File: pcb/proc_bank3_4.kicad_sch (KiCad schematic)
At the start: 2 parts, among them U1 XC6SLX9-TQG144

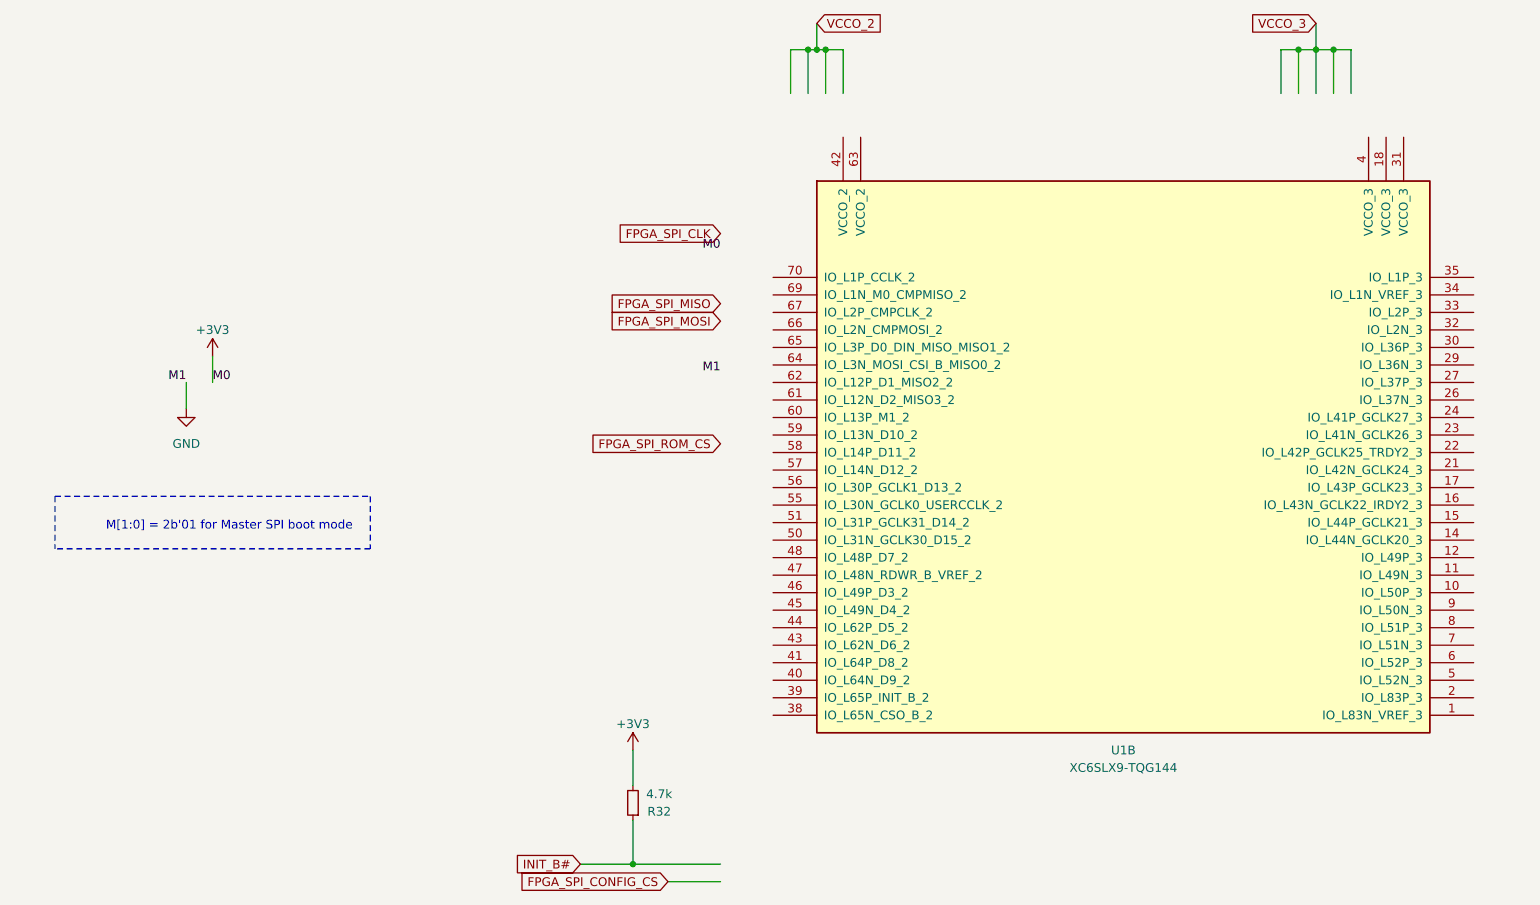
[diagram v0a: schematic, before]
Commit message: route pol
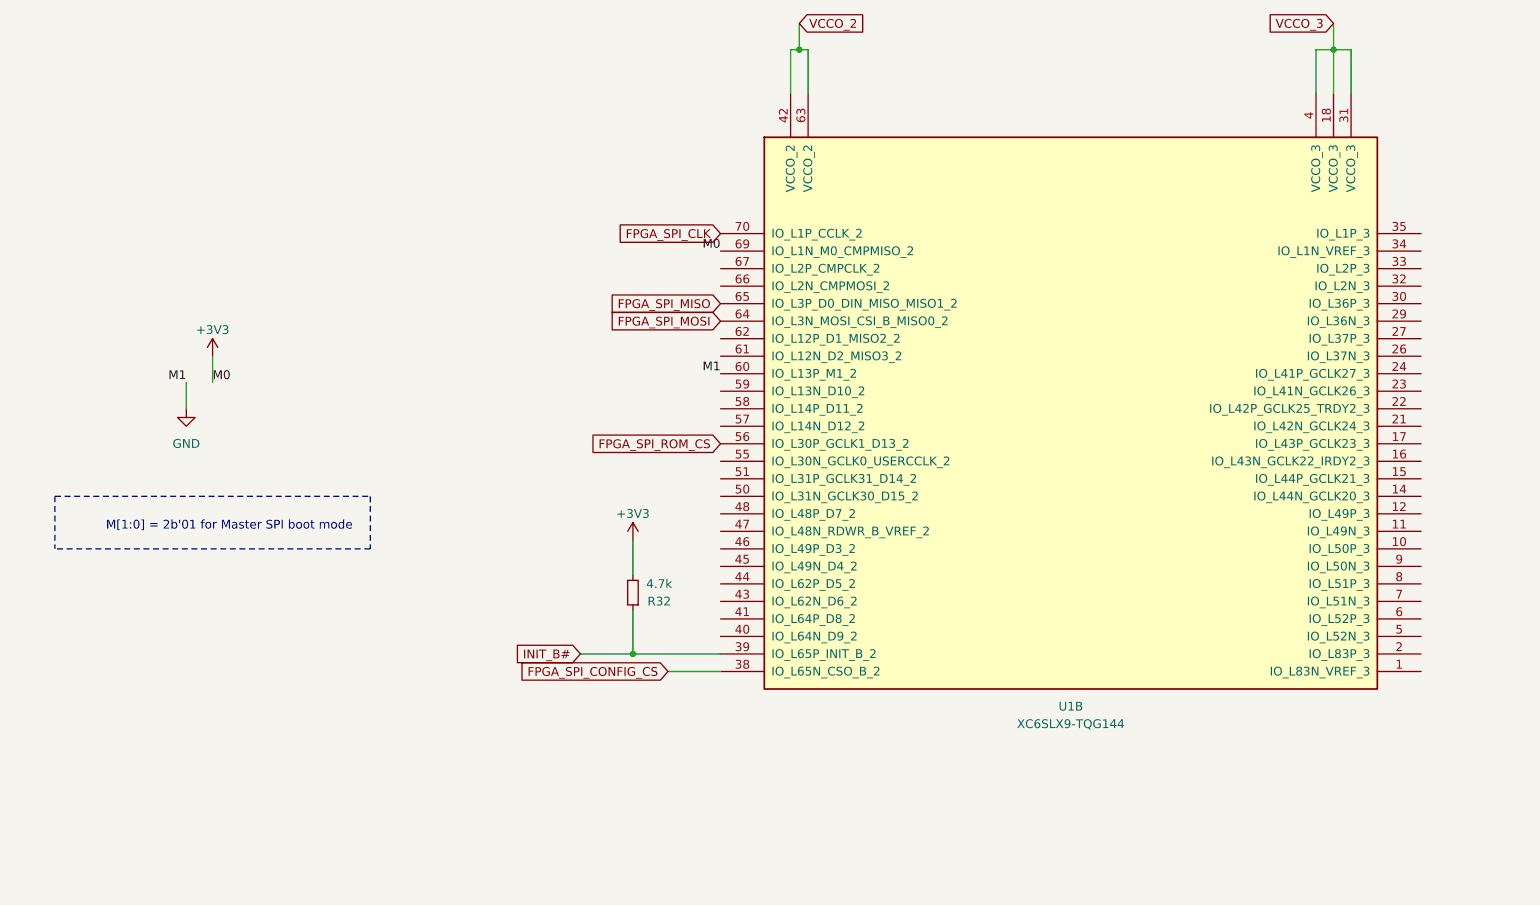
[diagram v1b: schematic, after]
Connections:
- net +3V3: now also U1.69 (IO_L1N_M0_CMPMISO_2)
- net FPGA_SPI_CLK: now also U1.70 (IO_L1P_CCLK_2)
- net FPGA_SPI_CONFIG_CS: now also U1.38 (IO_L65N_CSO_B_2)
- net FPGA_SPI_MISO: now also U1.65 (IO_L3P_D0_DIN_MISO_MISO1_2)
- net FPGA_SPI_MOSI: now also U1.64 (IO_L3N_MOSI_CSI_B_MISO0_2)
- net FPGA_SPI_ROM_CS: now also U1.56 (IO_L30P_GCLK1_D13_2)
- net GND: now also U1.60 (IO_L13P_M1_2)
- net INIT_B#: now also U1.39 (IO_L65P_INIT_B_2)
- net VCCO_2: now also U1.42 (VCCO_2), U1.63 (VCCO_2)
- net VCCO_3: now also U1.18 (VCCO_3), U1.31 (VCCO_3), U1.4 (VCCO_3)
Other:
- moved on the sheet: R32, U1B
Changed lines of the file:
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@@
 (kicad_sch (version 20210406) (generator eeschema)
-  (paper "User" 280.01 240.005)
-  (junction (at 121.92 147.32) (diameter 0.9144) (color 0 0 0 0))
-  (junction (at 147.32 29.21) (diameter 0.9144) (color 0 0 0 0))
-  (junction (at 148.59 29.21) (diameter 0.9144) (color 0 0 0 0))
-  (junction (at 149.86 29.21) (diameter 0.9144) (color 0 0 0 0))
-  (junction (at 218.44 29.21) (diameter 0.9144) (color 0 0 0 0))
-  (junction (at 220.98 29.21) (diameter 0.9144) (color 0 0 0 0))
+  (paper "User" 280.01 180.01)
+  (junction (at 121.92 116.84) (diameter 0.9144) (color 0 0 0 0))
+  (junction (at 146.05 29.21) (diameter 0.9144) (color 0 0 0 0))
   (junction (at 223.52 29.21) (diameter 0.9144) (color 0 0 0 0))
   (wire (pts (xy 57.15 77.47) (xy 57.15 81.28))
@@
     (stroke (width 0) (type solid) (color 0 0 0 0))
   )
-  (wire (pts (xy 114.3 147.32) (xy 121.92 147.32))
+  (wire (pts (xy 114.3 116.84) (xy 121.92 116.84))
     (stroke (width 0) (type solid) (color 0 0 0 0))
   )
-  (wire (pts (xy 121.92 130.81) (xy 121.92 135.89))
+  (wire (pts (xy 121.92 100.33) (xy 121.92 105.41))
     (stroke (width 0) (type solid) (color 0 0 0 0))
   )
-  (wire (pts (xy 121.92 147.32) (xy 121.92 140.97))
+  (wire (pts (xy 121.92 116.84) (xy 121.92 110.49))
     (stroke (width 0) (type solid) (color 0 0 0 0))
   )
-  (wire (pts (xy 127 149.86) (xy 134.62 149.86))
+  (wire (pts (xy 127 119.38) (xy 134.62 119.38))
     (stroke (width 0) (type solid) (color 0 0 0 0))
   )
-  (wire (pts (xy 134.62 147.32) (xy 121.92 147.32))
+  (wire (pts (xy 134.62 116.84) (xy 121.92 116.84))
     (stroke (width 0) (type solid) (color 0 0 0 0))
   )
-  (wire (pts (xy 144.78 29.21) (xy 147.32 29.21))
+  (wire (pts (xy 144.78 29.21) (xy 146.05 29.21))
     (stroke (width 0) (type solid) (color 0 0 0 0))
   )
@@
     (stroke (width 0) (type solid) (color 0 0 0 0))
   )
-  (wire (pts (xy 147.32 29.21) (xy 147.32 35.56))
+  (wire (pts (xy 146.05 25.4) (xy 146.05 29.21))
     (stroke (width 0) (type solid) (color 0 0 0 0))
   )
-  (wire (pts (xy 147.32 29.21) (xy 148.59 29.21))
+  (wire (pts (xy 146.05 29.21) (xy 147.32 29.21))
     (stroke (width 0) (type solid) (color 0 0 0 0))
   )
-  (wire (pts (xy 148.59 25.4) (xy 148.59 29.21))
-    (stroke (width 0) (type solid) (color 0 0 0 0))
-  )
-  (wire (pts (xy 149.86 29.21) (xy 148.59 29.21))
-    (stroke (width 0) (type solid) (color 0 0 0 0))
-  )
-  (wire (pts (xy 149.86 29.21) (xy 149.86 35.56))
-    (stroke (width 0) (type solid) (color 0 0 0 0))
-  )
-  (wire (pts (xy 149.86 29.21) (xy 152.4 29.21))
-    (stroke (width 0) (type solid) (color 0 0 0 0))
-  )
-  (wire (pts (xy 152.4 35.56) (xy 152.4 29.21))
-    (stroke (width 0) (type solid) (color 0 0 0 0))
-  )
-  (wire (pts (xy 215.9 29.21) (xy 215.9 35.56))
-    (stroke (width 0) (type solid) (color 0 0 0 0))
-  )
-  (wire (pts (xy 215.9 29.21) (xy 218.44 29.21))
-    (stroke (width 0) (type solid) (color 0 0 0 0))
-  )
-  (wire (pts (xy 218.44 29.21) (xy 218.44 35.56))
-    (stroke (width 0) (type solid) (color 0 0 0 0))
-  )
-  (wire (pts (xy 218.44 29.21) (xy 220.98 29.21))
-    (stroke (width 0) (type solid) (color 0 0 0 0))
-  )
-  (wire (pts (xy 220.98 25.4) (xy 220.98 29.21))
+  (wire (pts (xy 147.32 29.21) (xy 147.32 35.56))
     (stroke (width 0) (type solid) (color 0 0 0 0))
   )
@@
   )
   (wire (pts (xy 220.98 29.21) (xy 223.52 29.21))
+    (stroke (width 0) (type solid) (color 0 0 0 0))
+  )
+  (wire (pts (xy 223.52 25.4) (xy 223.52 29.21))
     (stroke (width 0) (type solid) (color 0 0 0 0))
   )
@@
     (effects (font (size 1.27 1.27)) (justify right bottom))
   )
-  (global_label "INIT_B#" (shape input) (at 114.3 147.32 180) (fields_autoplaced)
+  (global_label "INIT_B#" (shape input) (at 114.3 116.84 180) (fields_autoplaced)
     (effects (font (size 1.27 1.27)) (justify right))
-    (property "Intersheet References" "${INTERSHEET_REFS}" (id 0) (at 104.8717 147.2406 0)
+    (property "Intersheet References" "${INTERSHEET_REFS}" (id 0) (at 104.8717 116.7606 0)
       (effects (font (size 1.27 1.27)) (justify right) hide)
     )
   )
-  (global_label "FPGA_SPI_CONFIG_CS" (shape input) (at 127 149.86 180) (fields_autoplaced)
+  (global_label "FPGA_SPI_CONFIG_CS" (shape input) (at 127 119.38 180) (fields_autoplaced)
     (effects (font (size 1.27 1.27)) (justify right))
-    (property "Intersheet References" "${INTERSHEET_REFS}" (id 0) (at 104.5088 149.7806 0)
+    (property "Intersheet References" "${INTERSHEET_REFS}" (id 0) (at 104.5088 119.3006 0)
       (effects (font (size 1.27 1.27)) (justify right) hide)
     )
@@
     )
   )
-  (global_label "VCCO_2" (shape input) (at 148.59 25.4 0) (fields_autoplaced)
+  (global_label "VCCO_2" (shape input) (at 146.05 25.4 0) (fields_autoplaced)
     (effects (font (size 1.27 1.27)) (justify left))
-    (property "Intersheet References" "${INTERSHEET_REFS}" (id 0) (at 158.1393 25.3206 0)
+    (property "Intersheet References" "${INTERSHEET_REFS}" (id 0) (at 155.5993 25.3206 0)
       (effects (font (size 1.27 1.27)) (justify left) hide)
     )
   )
-  (global_label "VCCO_3" (shape input) (at 220.98 25.4 180) (fields_autoplaced)
+  (global_label "VCCO_3" (shape input) (at 223.52 25.4 180) (fields_autoplaced)
     (effects (font (size 1.27 1.27)) (justify right))
-    (property "Intersheet References" "${INTERSHEET_REFS}" (id 0) (at 211.4307 25.3206 0)
+    (property "Intersheet References" "${INTERSHEET_REFS}" (id 0) (at 213.9707 25.3206 0)
       (effects (font (size 1.27 1.27)) (justify right) hide)
     )
@@
     (pin "1")
   )
-  (symbol (lib_id "power:+3V3") (at 121.92 130.81 0) (unit 1)
+  (symbol (lib_id "power:+3V3") (at 121.92 100.33 0) (unit 1)
     (in_bom yes) (on_board yes) (fields_autoplaced)
-    (property "Reference" "#PWR089" (id 0) (at 121.92 134.62 0)
+    (property "Reference" "#PWR089" (id 0) (at 121.92 104.14 0)
       (effects (font (size 1.27 1.27)) hide)
     )
-    (property "Value" "+3V3" (id 1) (at 121.92 127 0))
-    (property "Footprint" "" (id 2) (at 121.92 130.81 0)
+    (property "Value" "+3V3" (id 1) (at 121.92 96.52 0))
+    (property "Footprint" "" (id 2) (at 121.92 100.33 0)
       (effects (font (size 1.27 1.27)) hide)
     )
-    (property "Datasheet" "" (id 3) (at 121.92 130.81 0)
+    (property "Datasheet" "" (id 3) (at 121.92 100.33 0)
       (effects (font (size 1.27 1.27)) hide)
     )
@@
     (pin "1")
   )
-  (symbol (lib_id "Device:R_Small") (at 121.92 138.43 180) (unit 1)
+  (symbol (lib_id "Device:R_Small") (at 121.92 107.95 180) (unit 1)
     (in_bom yes) (on_board yes)
-    (property "Reference" "R32" (id 0) (at 125.73 139.7 0))
-    (property "Value" "4.7k" (id 1) (at 125.73 137.16 0))
-    (property "Footprint" "Resistor_SMD:R_0402_1005Metric" (id 2) (at 121.92 138.43 0)
+    (property "Reference" "R32" (id 0) (at 125.73 109.22 0))
+    (property "Value" "4.7k" (id 1) (at 125.73 106.68 0))
+    (property "Footprint" "Resistor_SMD:R_0402_1005Metric" (id 2) (at 121.92 107.95 0)
       (effects (font (size 1.27 1.27)) hide)
     )
-    (property "Datasheet" "~" (id 3) (at 121.92 138.43 0)
+    (property "Datasheet" "~" (id 3) (at 121.92 107.95 0)
       (effects (font (size 1.27 1.27)) hide)
     )
@@
     (pin "2")
   )
-  (symbol (lib_id "FPGA_Xilinx_Spartan6:XC6SLX9-TQG144") (at 193.04 85.09 0) (unit 2)
+  (symbol (lib_id "FPGA_Xilinx_Spartan6:XC6SLX9-TQG144") (at 185.42 78.74 0) (unit 2)
     (in_bom yes) (on_board yes) (fields_autoplaced)
-    (property "Reference" "U1" (id 0) (at 193.04 130.81 0))
-    (property "Value" "XC6SLX9-TQG144" (id 1) (at 193.04 133.35 0))
-    (property "Footprint" "Package_QFP:TQFP-144_20x20mm_P0.5mm" (id 2) (at 193.04 85.09 0)
+    (property "Reference" "U1" (id 0) (at 185.42 124.46 0))
+    (property "Value" "XC6SLX9-TQG144" (id 1) (at 185.42 127 0))
+    (property "Footprint" "Package_QFP:TQFP-144_20x20mm_P0.5mm" (id 2) (at 185.42 78.74 0)
       (effects (font (size 1.27 1.27)) hide)
     )
-    (property "Datasheet" "" (id 3) (at 193.04 85.09 0))
+    (property "Datasheet" "" (id 3) (at 185.42 78.74 0))
     (pin "1")
     (pin "10")

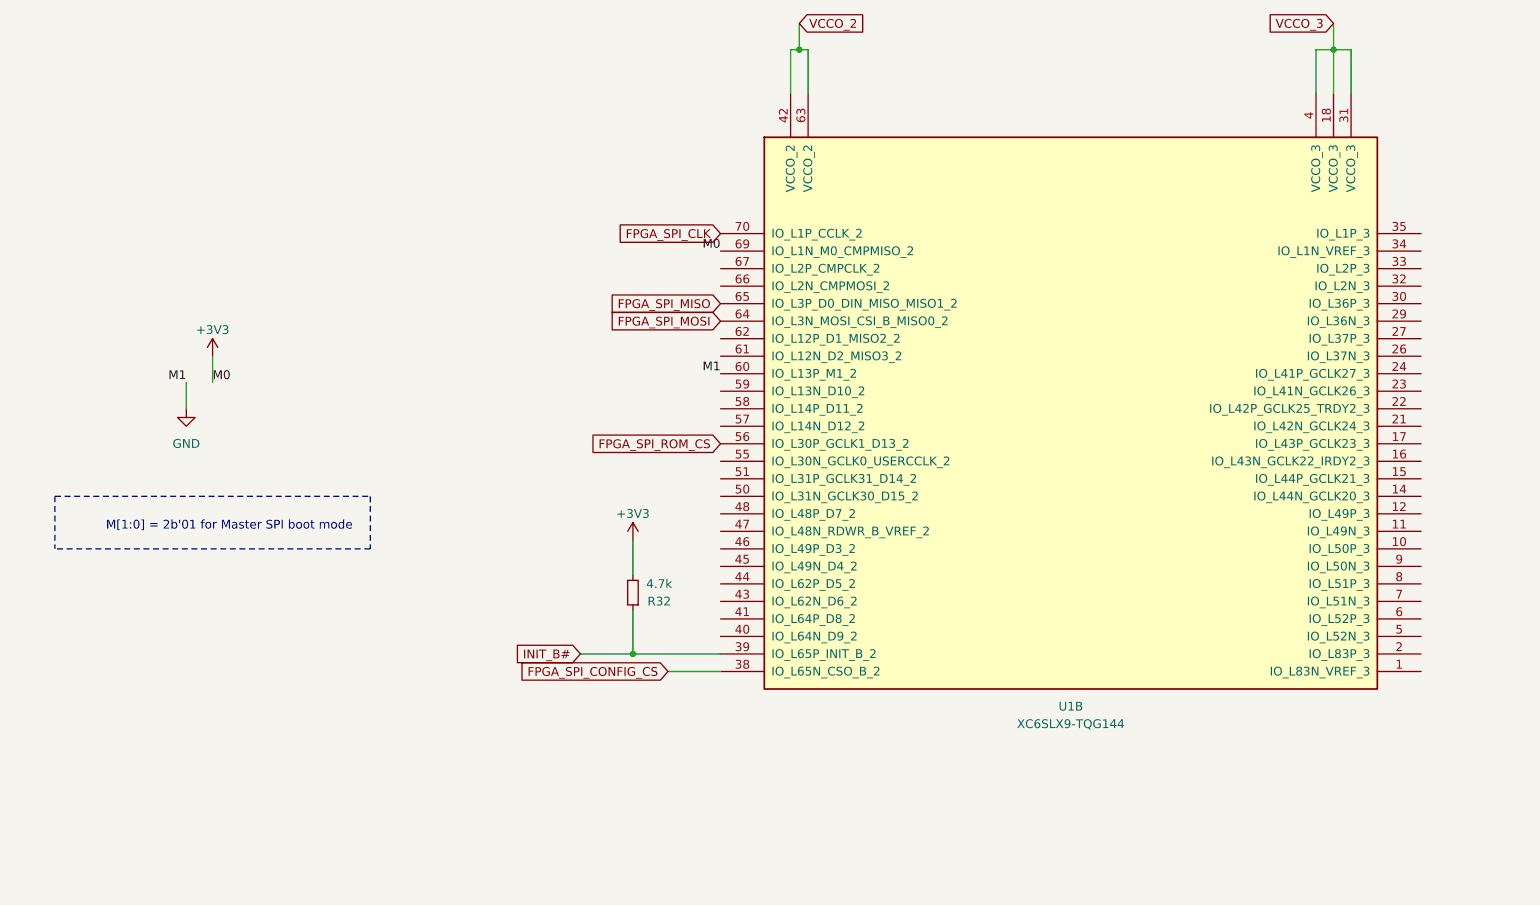
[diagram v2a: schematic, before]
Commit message: added silkscreen values
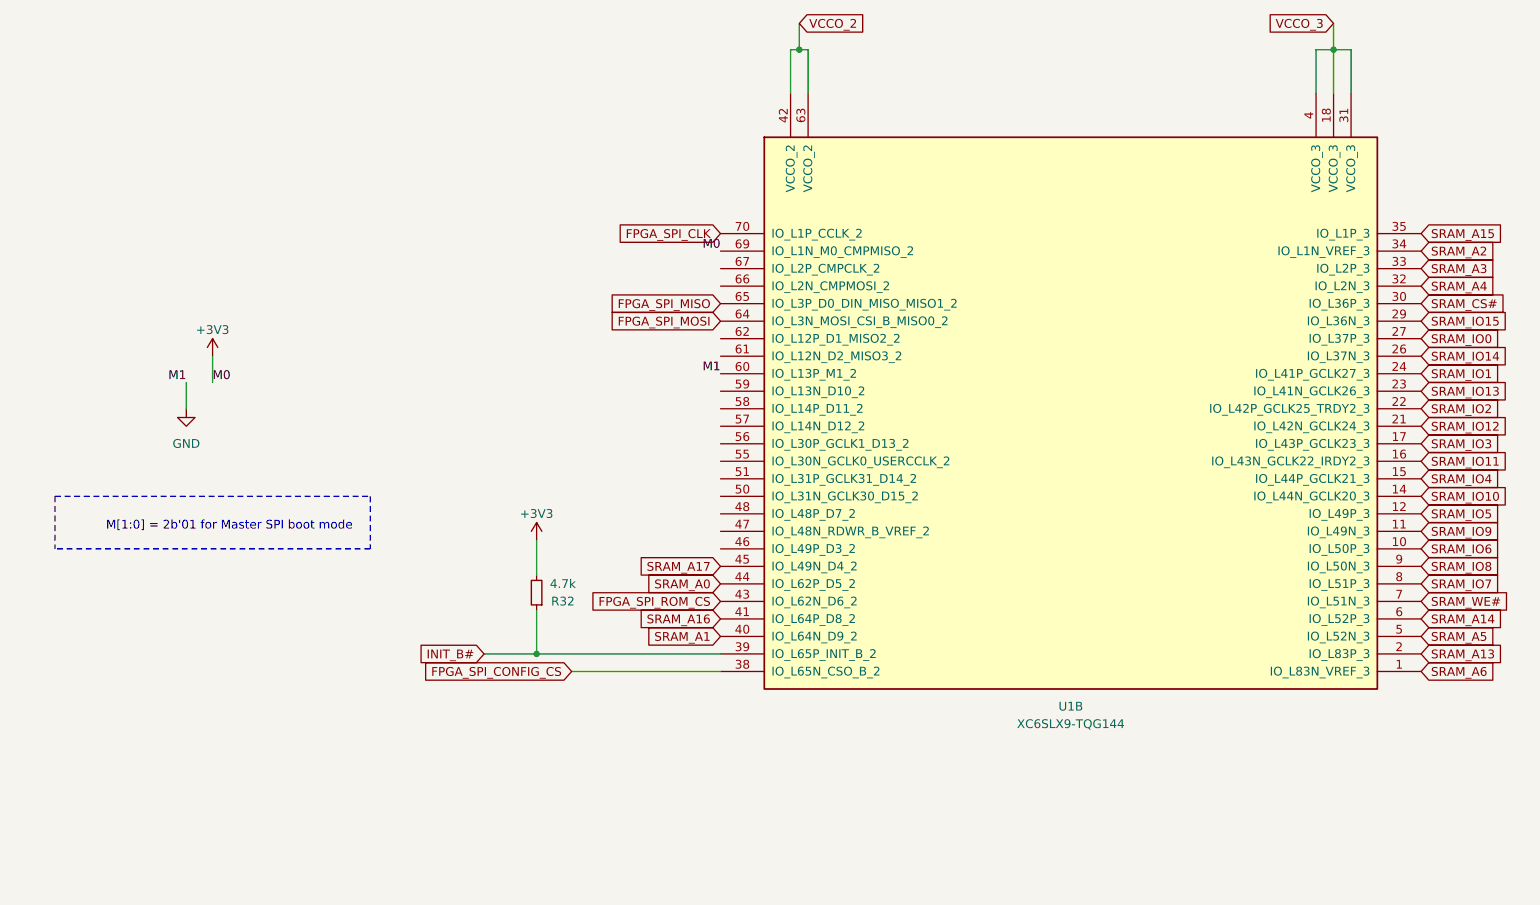
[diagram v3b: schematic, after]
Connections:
- net FPGA_SPI_ROM_CS: now also U1.43 (IO_L62N_D6_2); no longer U1.56 (IO_L30P_GCLK1_D13_2)
- net SRAM_A6: now reaches U1.1 (IO_L83N_VREF_3)
- net SRAM_IO6: now reaches U1.10 (IO_L50P_3)
- net SRAM_IO9: now reaches U1.11 (IO_L49N_3)
- net SRAM_IO5: now reaches U1.12 (IO_L49P_3)
- net SRAM_IO10: now reaches U1.14 (IO_L44N_GCLK20_3)
- net SRAM_IO4: now reaches U1.15 (IO_L44P_GCLK21_3)
- net SRAM_IO11: now reaches U1.16 (IO_L43N_GCLK22_IRDY2_3)
- net SRAM_IO3: now reaches U1.17 (IO_L43P_GCLK23_3)
- net SRAM_A13: now reaches U1.2 (IO_L83P_3)
- net SRAM_IO12: now reaches U1.21 (IO_L42N_GCLK24_3)
- net SRAM_IO2: now reaches U1.22 (IO_L42P_GCLK25_TRDY2_3)
- net SRAM_IO13: now reaches U1.23 (IO_L41N_GCLK26_3)
- net SRAM_IO1: now reaches U1.24 (IO_L41P_GCLK27_3)
- net SRAM_IO14: now reaches U1.26 (IO_L37N_3)
- net SRAM_IO0: now reaches U1.27 (IO_L37P_3)
- net SRAM_IO15: now reaches U1.29 (IO_L36N_3)
- net SRAM_CS#: now reaches U1.30 (IO_L36P_3)
- net SRAM_A4: now reaches U1.32 (IO_L2N_3)
- net SRAM_A3: now reaches U1.33 (IO_L2P_3)
- net SRAM_A2: now reaches U1.34 (IO_L1N_VREF_3)
- net SRAM_A15: now reaches U1.35 (IO_L1P_3)
- net SRAM_A1: now reaches U1.40 (IO_L64N_D9_2)
- net SRAM_A16: now reaches U1.41 (IO_L64P_D8_2)
- net SRAM_A0: now reaches U1.44 (IO_L62P_D5_2)
- net SRAM_A17: now reaches U1.45 (IO_L49N_D4_2)
- net SRAM_A5: now reaches U1.5 (IO_L52N_3)
- net SRAM_A14: now reaches U1.6 (IO_L52P_3)
- net SRAM_WE#: now reaches U1.7 (IO_L51N_3)
- net SRAM_IO7: now reaches U1.8 (IO_L51P_3)
- net SRAM_IO8: now reaches U1.9 (IO_L50N_3)
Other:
- moved on the sheet: R32
